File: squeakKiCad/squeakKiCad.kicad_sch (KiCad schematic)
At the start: 20 parts, among them J1 Conn_01x06_Pin, U1 KB2040, U2 BA00JC5WT, U3 PMW3360DM-T2QU

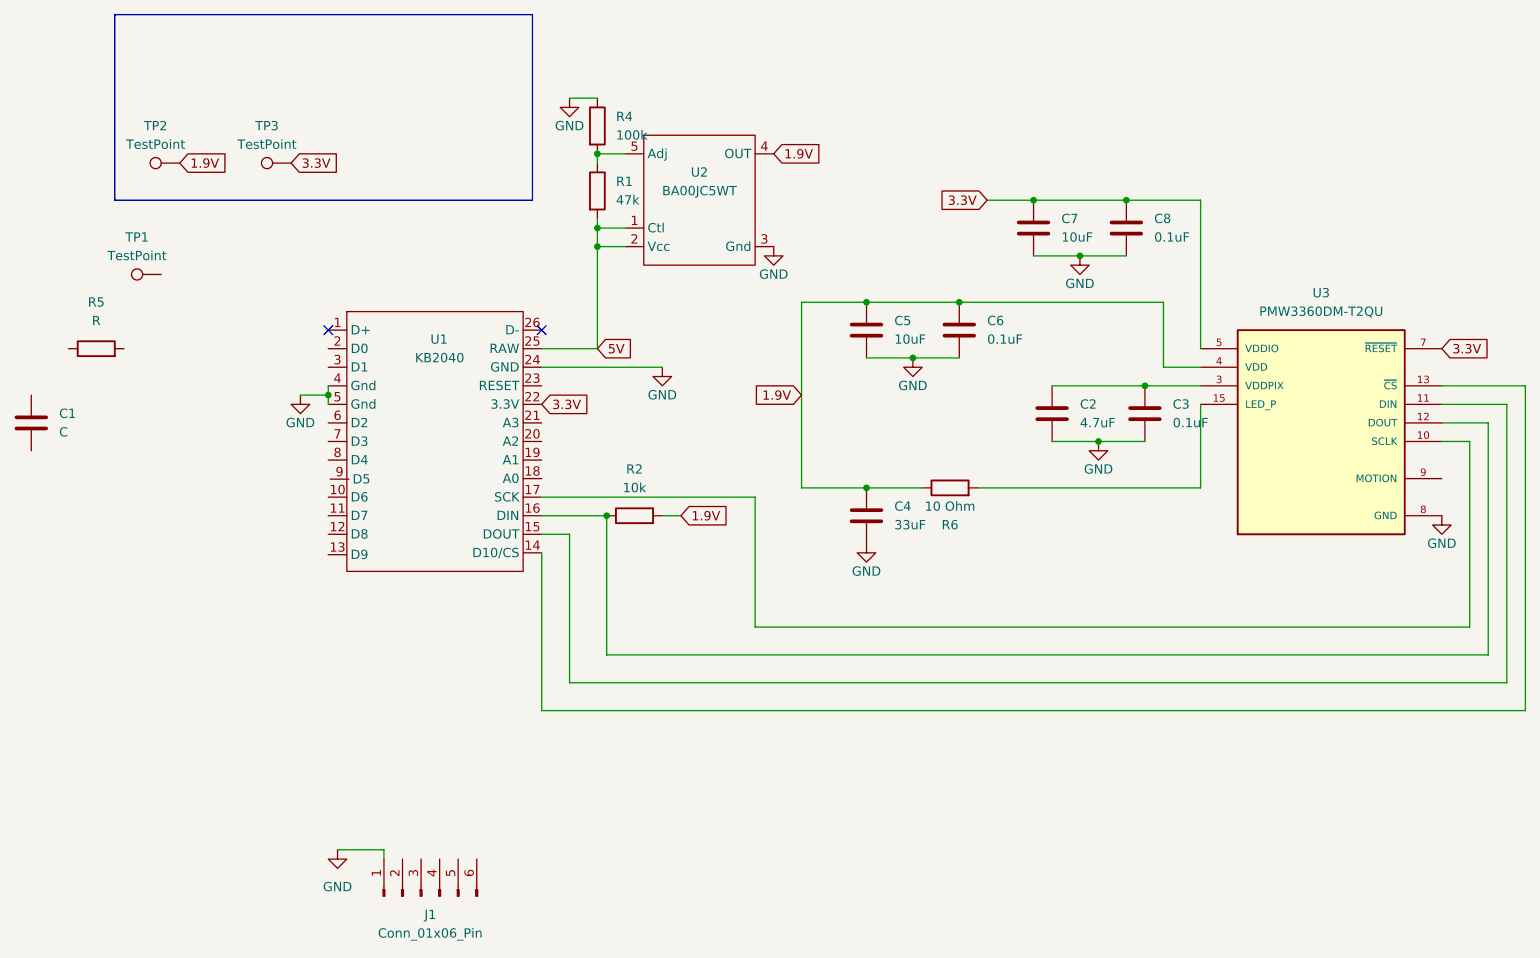
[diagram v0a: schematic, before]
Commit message: add draft of printable shell
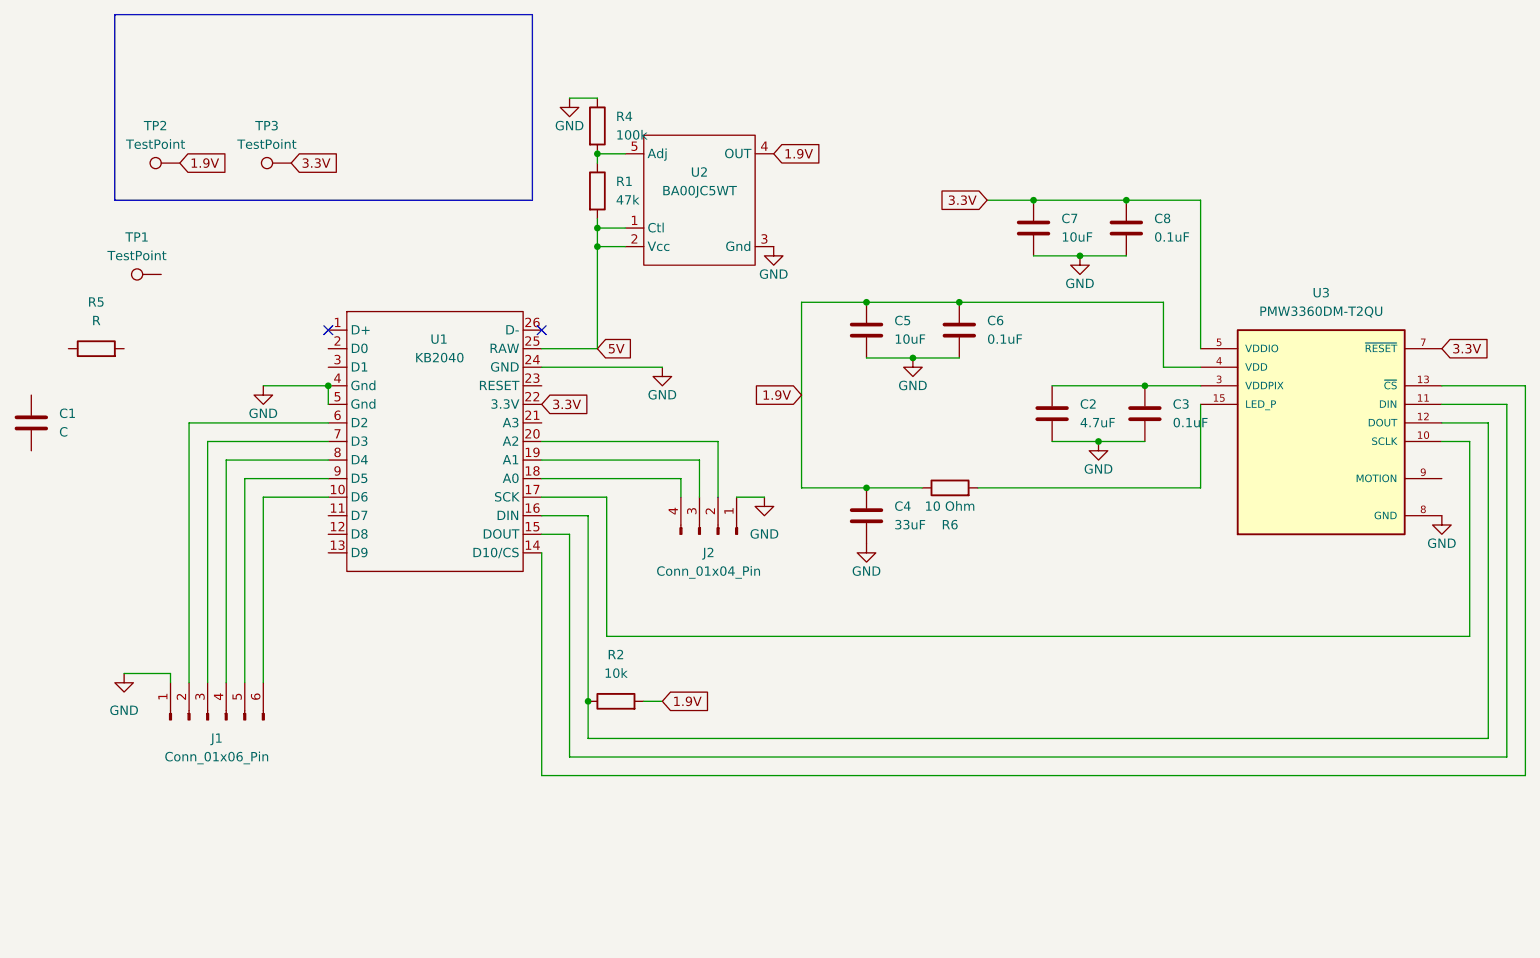
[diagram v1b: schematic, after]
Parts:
- added J2: Conn_01x04_Pin, Connector_JST:JST_XH_B4B-XH-A_1x04_P2.50mm_Vertical, symbol Connector:Conn_01x04_Pin
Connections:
- net GND: now also J2.1 (Pin_1)
- net at J1.2 (Pin_2): now also U1.6 (D2)
- net at J1.3 (Pin_3): now also U1.7 (D3)
- net at J1.4 (Pin_4): now also U1.8 (D4)
- net at J1.5 (Pin_5): now also U1.9 (D5)
- net at J1.6 (Pin_6): now also U1.10 (D6)
- net at U1.18 (A0): now also J2.4 (Pin_4)
- net at U1.19 (A1): now also J2.3 (Pin_3)
- net at U1.20 (A2): now also J2.2 (Pin_2)
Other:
- moved on the sheet: J1, R2

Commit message: revised schematic: sensor pins at wrong voltage
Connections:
- net 1.9V: now also C7.1, C8.1, U3.5 (VDDIO), U3.7 (~{RESET}); no longer R2.2
- net 3.3V: now also R2.2; no longer C7.1, C8.1, U3.5 (VDDIO), U3.7 (~{RESET})
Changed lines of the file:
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@@
     (fill (type none))
+  )
+  (global_label "1.9V" (shape input) (at 213.36 76.2 0) (fields_autoplaced)
+    (effects (font (size 1.27 1.27)) (justify left))
+    (property "Intersheetrefs" "${INTERSHEET_REFS}" (at 220.4576 76.2 0)
+      (effects (font (size 1.27 1.27)) (justify left) hide)
+    )
+  )
+  (global_label "1.9V" (shape input) (at 151.13 55.88 180) (fields_autoplaced)
+    (effects (font (size 1.27 1.27)) (justify right))
+    (property "Intersheetrefs" "${INTERSHEET_REFS}" (at 144.0324 55.88 0)
+      (effects (font (size 1.27 1.27)) (justify right) hide)
+    )
   )
   (global_label "5V" (shape input) (at 97.79 76.2 0) (fields_autoplaced)
     (effects (font (size 1.27 1.27)) (justify left))
     (property "Intersheetrefs" "${INTERSHEET_REFS}" (at 103.0733 76.2 0)
-      (effects (font (size 1.27 1.27)) (justify left) hide)
-    )
-  )
-  (global_label "1.9V" (shape input) (at 106.68 124.46 0) (fields_autoplaced)
-    (effects (font (size 1.27 1.27)) (justify left))
-    (property "Intersheetrefs" "${INTERSHEET_REFS}" (at 113.7776 124.46 0)
       (effects (font (size 1.27 1.27)) (justify left) hide)
     )
@@
     )
   )
-  (global_label "3.3V" (shape input) (at 151.13 55.88 180) (fields_autoplaced)
-    (effects (font (size 1.27 1.27)) (justify right))
-    (property "Intersheetrefs" "${INTERSHEET_REFS}" (at 144.0324 55.88 0)
-      (effects (font (size 1.27 1.27)) (justify right) hide)
-    )
-  )
   (global_label "3.3V" (shape input) (at 55.88 50.8 0) (fields_autoplaced)
     (effects (font (size 1.27 1.27)) (justify left))
@@
     )
   )
-  (global_label "3.3V" (shape input) (at 213.36 76.2 0) (fields_autoplaced)
+  (global_label "3.3V" (shape input) (at 106.68 124.46 0) (fields_autoplaced)
     (effects (font (size 1.27 1.27)) (justify left))
-    (property "Intersheetrefs" "${INTERSHEET_REFS}" (at 220.4576 76.2 0)
+    (property "Intersheetrefs" "${INTERSHEET_REFS}" (at 113.7776 124.46 0)
       (effects (font (size 1.27 1.27)) (justify left) hide)
     )
